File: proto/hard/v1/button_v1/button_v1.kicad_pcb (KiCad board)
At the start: 2 copper layers, 108.9 x 76.9 mm, 140 parts, among them J1 Conn_01x06_Female, J10 Conn_01x01_Female, J11 Conn_01x01_Female, J12 Conn_01x01_Female, J13 Conn_01x01_Female, J14 K3-2336D-combi, J15 Conn_01x03_Male, J16 Conn_01x01_Male, J2 Conn_01x06_Female, J3 Conn_01x06_Female, J4 Conn_01x06_Female, J5 USB_B_Micro, J6 Conn_01x08_Female, J7 Conn_01x04_Female, J8 AudioJack3, J9 Conn_01x01_Female, Q1 TP0610T, Q2 IRLML2060, Q3 TP0610T, Q4 IRLML2060, Q5 IRLML2060, Q6 UMG8N, Q7 UMG8N, Q8 TP0610T, U1 LCD_2.8_SPI, U10 NL27WZ14, U11 TC305, U12 OLED_0.96_I2C, U13 74HC595, U2 STM32F103C8Tx, U3 RT8009-33, U4 RClamp0554S, U5 RT9293, U7 AP1117-33, U8 485, U9 LM358, Y1 8MHz

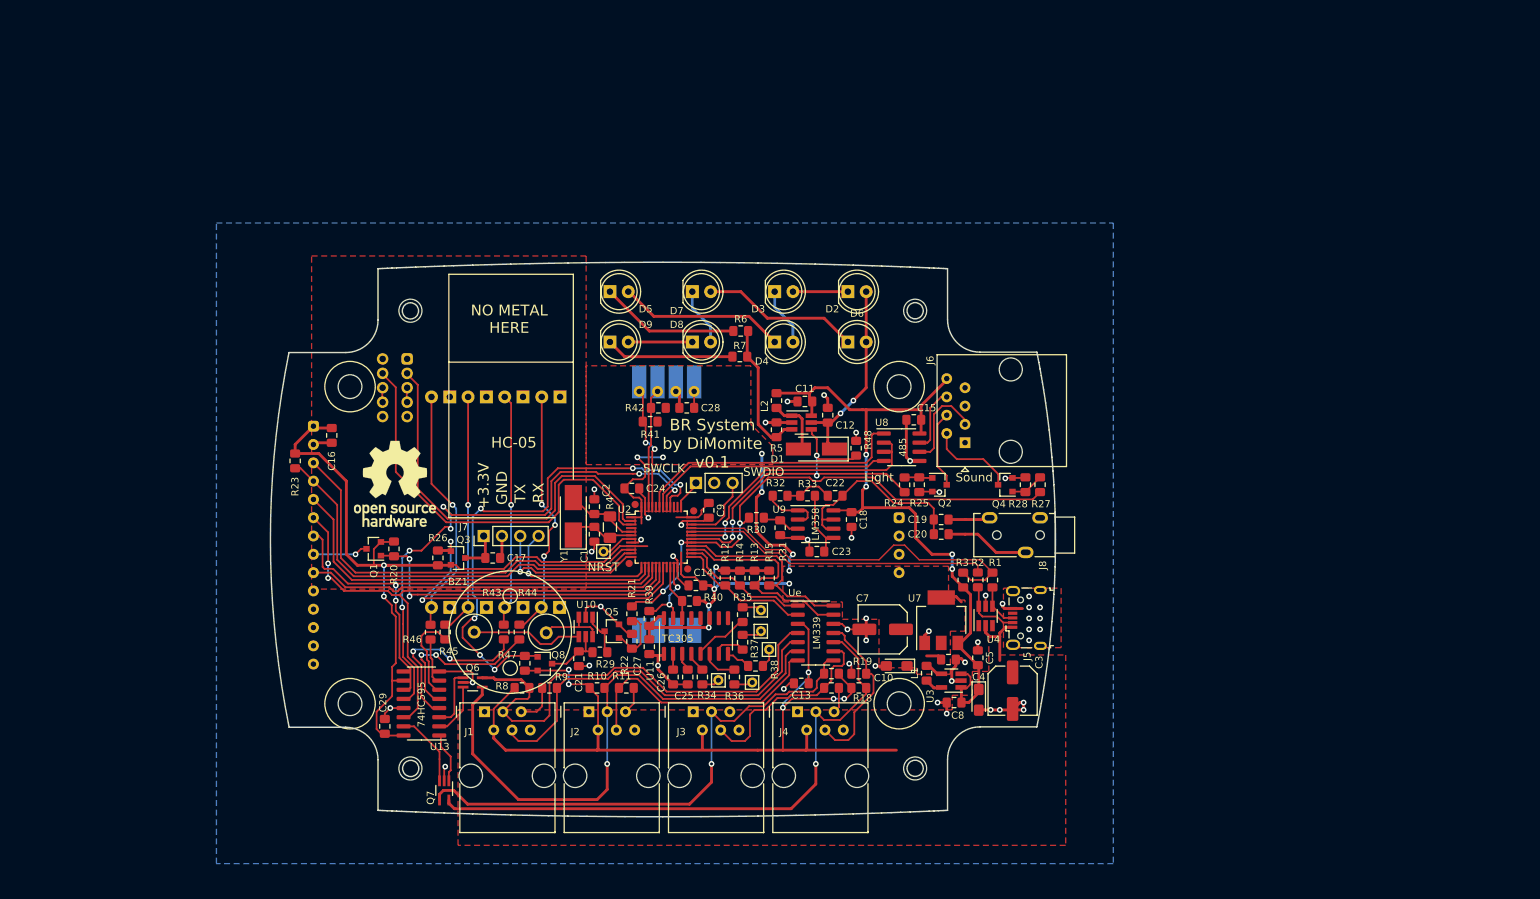
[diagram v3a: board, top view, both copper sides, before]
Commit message: Started schematic and PCB rework. Generated button_v1.pdf was left out of sync intentionally.
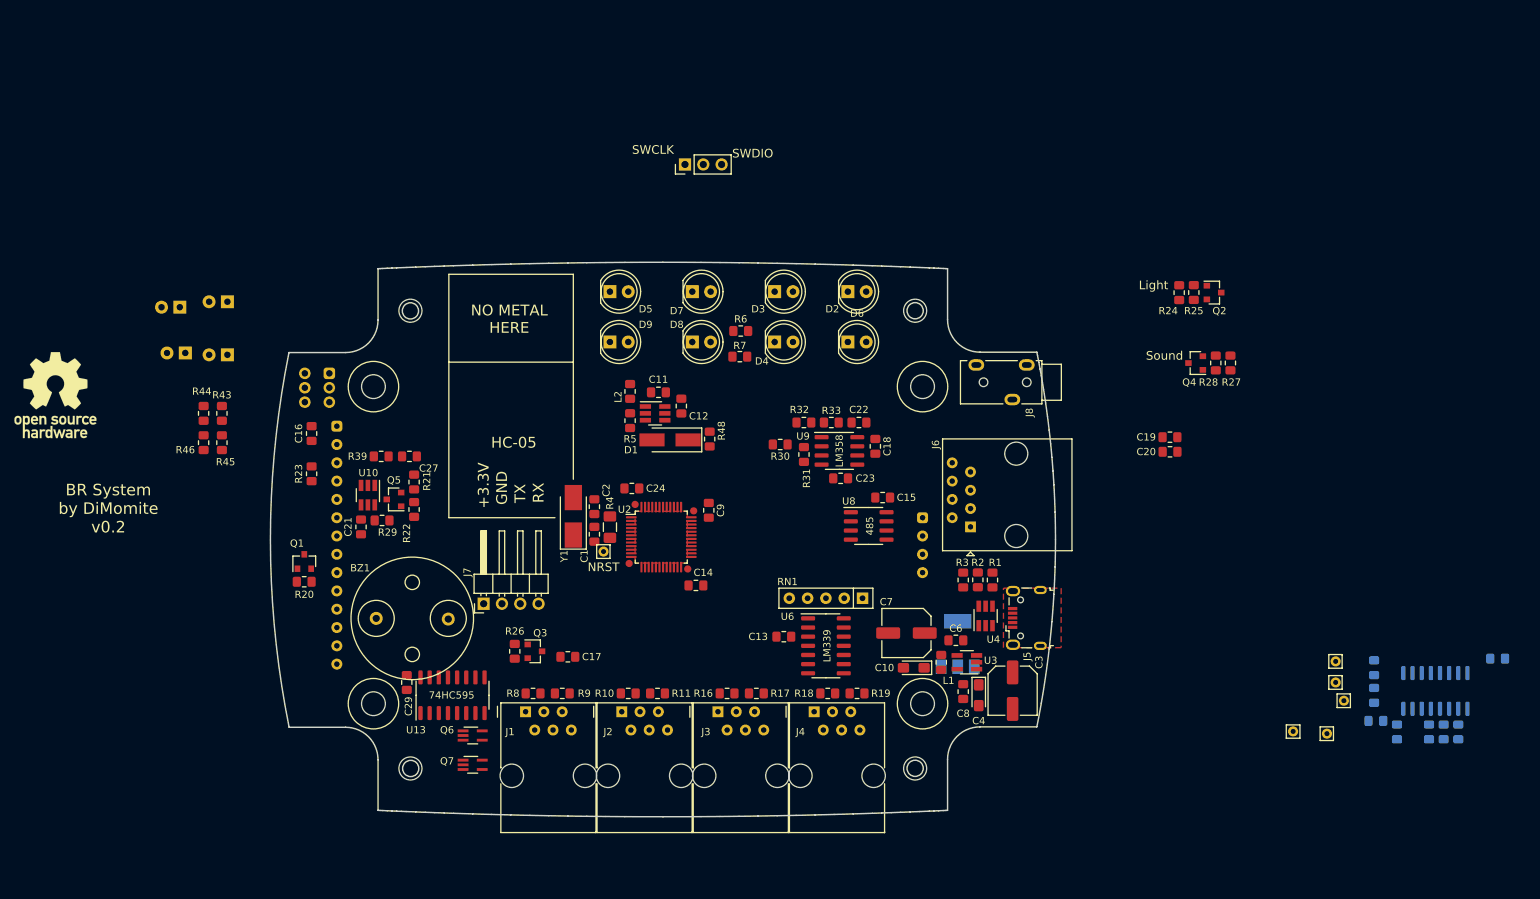
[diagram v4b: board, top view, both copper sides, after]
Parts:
- removed C28: 0.1uF, Capacitor_SMD:C_0805_2012Metric_Pad1.15x1.40mm_HandSolder
- removed C5: 1uF, Capacitor_SMD:C_0805_2012Metric_Pad1.15x1.40mm_HandSolder
- removed D14, D15, D16, D17: LED, LED_THT:LED_D3.0mm_Clear
- removed Q8: TP0610T, Package_TO_SOT_SMD:SOT-23
- removed R12, R13, R14, R15, R41, R42: 4k7, Resistor_SMD:R_0805_2012Metric_Pad1.15x1.40mm_HandSolder
- removed R47: 47k, Resistor_SMD:R_0805_2012Metric_Pad1.15x1.40mm_HandSolder
- removed U12: OLED_0.96_I2C, MyModules:OLED_0.96_I2C
- added RN1: 4k7, Resistor_THT:R_Array_SIP5, F.Cu at (150.6, 100.3)
- C25, C26, R34, R35, R36, R37, R38, R40, U11, U7: moved to B.Cu
- J14: value K3-2336D-combi -> K3-2235D; footprint brbuttonsystem:K3-2346D -> brbuttonsystem:K3-2235D
- J7: footprint Connector_PinHeader_2.54mm:PinHeader_1x04_P2.54mm_Vertical -> Connector_PinHeader_2.54mm:PinHeader_1x04_P2.54mm_Horizontal
- moved R40 112.4 mm to (238.8, 108.7)
- moved C26 109.2 mm to (233.3, 118.9)
- moved C25 105.2 mm to (231.3, 118.9)
- moved U11 102.9 mm to (230.1, 113.2)
- moved R34 101.1 mm to (229.2, 118.9)
- moved R36 92.3 mm to (224.8, 118.9)
- moved R35 87.9 mm to (221.6, 110.0)
- moved R37 87.9 mm to (221.6, 113.8)
- moved R38 86.4 mm to (221.9, 117.3), turned to 180 degrees
- moved J10 80.1 mm to (216.3, 109.1)
- moved J11 80.1 mm to (215.1, 119.1)
- moved J12 80.1 mm to (216.3, 112.0)
- moved J13 80.1 mm to (217.4, 114.6)
- moved J9 80.1 mm to (210.4, 118.8)
- moved D10 58.7 mm to (56.6, 66.3)
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- renumbered Ue to U6
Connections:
- C21 pad 1: /Entertainment/BuzzerPower -> Net-(C21-Pad1)
- J14 pad 4: Net-(J14-Pad4) -> GND
- J14 pad 5: GND -> Net-(J14-Pad5)
- J14 pad 6: Net-(J14-Pad10) -> Net-(J14-Pad6)
- Q6 pad 4: Net-(J2-Pad3) -> Net-(J2-Pad4)
- Q6 pad 5: Net-(J1-Pad3) -> Net-(J1-Pad4)
- Q7 pad 4: Net-(J3-Pad3) -> Net-(J4-Pad4)
- Q7 pad 5: Net-(J4-Pad3) -> Net-(J3-Pad4)
- R29 pad 2: /Entertainment/BuzzerPower -> +5V
- U10 pad 5: /Entertainment/BuzzerPower -> +5V
- U2 pad 3: /Touch4Front -> Net-(U2-Pad3)
- U2 pad 40: /BuzzerEnable -> Net-(U2-Pad40)
- U2 pad 45: /DISP_SCL -> Net-(U2-Pad45)
- U2 pad 46: /DISP_SDA -> Net-(U2-Pad46)
- U6 pad 10: Net-(J4-Pad3) -> Net-(J4-Pad4)
- U6 pad 11: Net-(J4-Pad4) -> Net-(J4-Pad3)
- U6 pad 4: Net-(J1-Pad3) -> Net-(J1-Pad4)
- U6 pad 5: Net-(J1-Pad4) -> Net-(J1-Pad3)
- U6 pad 6: Net-(J2-Pad3) -> Net-(J2-Pad4)
- U6 pad 7: Net-(J2-Pad4) -> Net-(J2-Pad3)
- U6 pad 8: Net-(J3-Pad3) -> Net-(J3-Pad4)
- U6 pad 9: Net-(J3-Pad4) -> Net-(J3-Pad3)
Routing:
- net +5V: track 236.4 -> 0.00 mm, vias 10 -> 0
- net +3V3: track 210.8 -> 0.00 mm, vias 13 -> 0
- net GND: track 138.3 -> 0.00 mm, vias 47 -> 0
- net Net-(J4-Pad3): track 81.6 -> 0.00 mm, vias 1 -> 0
- net Net-(J2-Pad3): track 78.8 -> 0.00 mm, vias 1 -> 0
- net /LCD_MOSI: track 77.8 -> 0.00 mm, vias 2 -> 0
- net /EXTRA_TICK: track 75.0 -> 0.00 mm, vias 6 -> 0
- net /Sound_PWM: track 73.4 -> 0.00 mm, vias 4 -> 0
- net Net-(J3-Pad3): track 73.1 -> 0.00 mm, vias 1 -> 0
- net /LCD_SCK: track 70.6 -> 0.00 mm, vias 2 -> 0
- net /BuzzerEnable: track 70.5 -> 0.00 mm, vias 6 -> 0
- net Net-(J1-Pad3): track 66.6 -> 0.00 mm
- net /LCD_RESET: track 59.1 -> 0.00 mm
- net /Touch4Front: track 58.4 -> 0.00 mm
- net /LCD_CS: track 57.7 -> 0.00 mm
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- removed copper zone on F.Cu, net +5V
- removed copper zone on B.Cu, net GND
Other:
- board text added: "!!! Offset by 4 mm from center !!!"
- board text added: "BR System by DiMomite v0.2"
- board text removed: "BR System by DiMomite v0.1"

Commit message: PCB rework in progress. Centered main LCD. Added second LCD. Button connectors we shifted to the right.
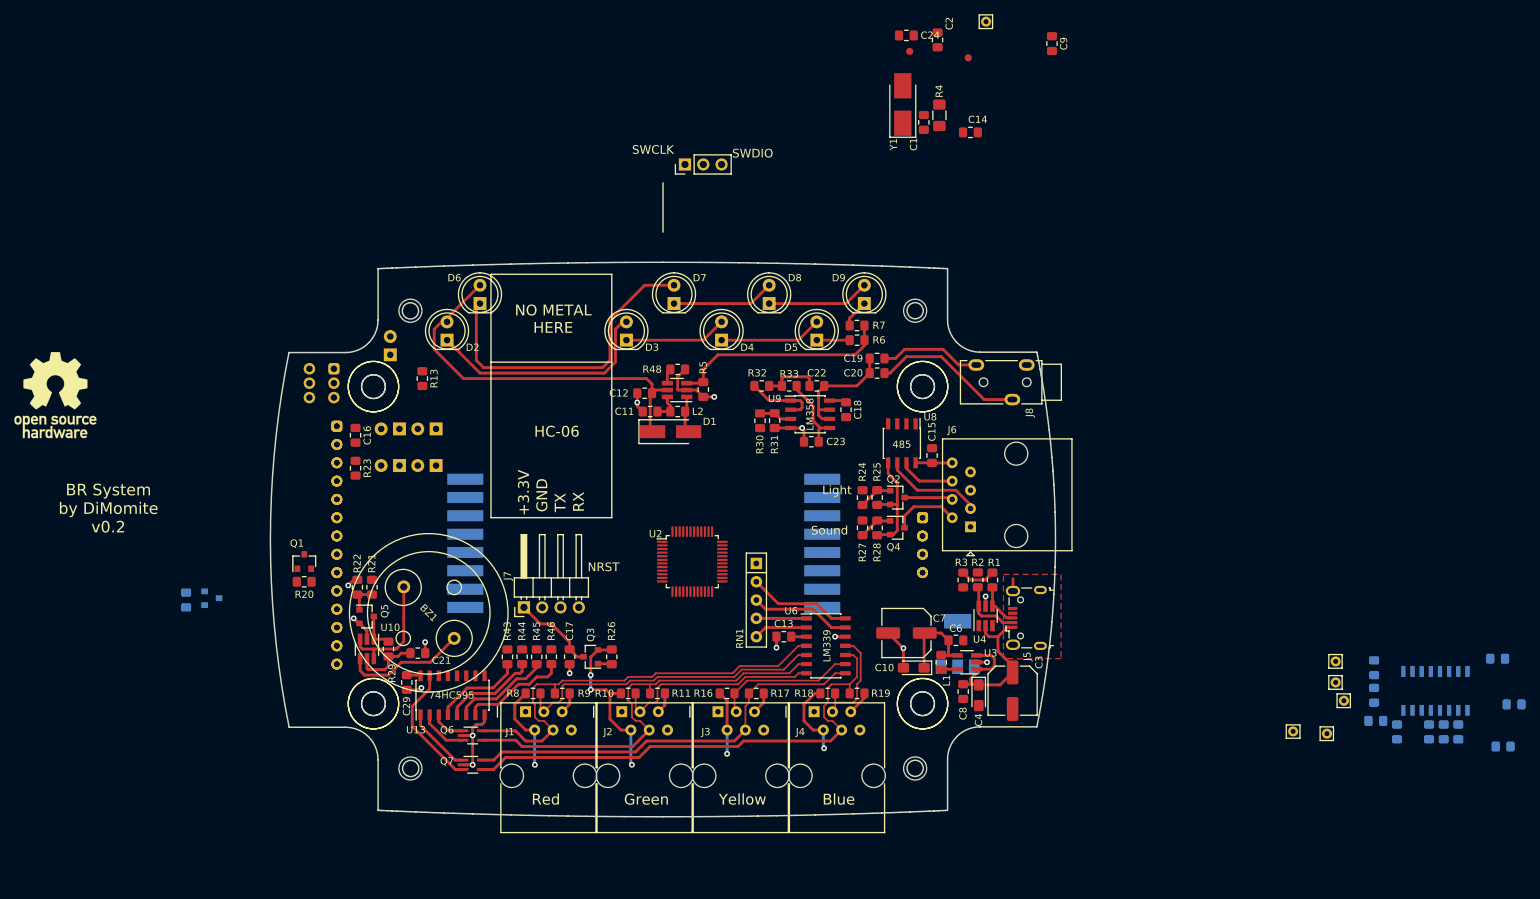
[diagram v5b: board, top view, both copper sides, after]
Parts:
- added D14: LED, LED_THT:LED_D3.0mm_Clear, B.Cu at (85.1, 66.5)
- added Q8: IRLML2803, Package_TO_SOT_SMD:SOT-23, B.Cu at (60.3, 100.3)
- added R12: 47k, Resistor_SMD:R_0805_2012Metric_Pad1.15x1.40mm_HandSolder, B.Cu at (56.8, 100.6)
- added R13: 1k, Resistor_SMD:R_0805_2012Metric_Pad1.15x1.40mm_HandSolder, F.Cu at (89.5, 69.8)
- added U1: LCD_2.8_SPI, MyModules:LCD_2.8_SPI, F.Cu at (77.7, 93.0)
- added U12: LCD_1_8_SPI, brbuttonsystem:LCD_1_8_SPI, B.Cu at (95.5, 92.7)
- BZ1: footprint MyModules:buzz17 -> brbuttonsystem:buzz17
- C27, R39: moved to B.Cu
- moved R39 160.9 mm to (241.0, 115.1)
- moved C27 157.0 mm to (239.5, 120.9)
- moved J16 90.7 mm to (167.8, 20.3)
- moved C9 80.4 mm to (176.9, 23.4)
- moved C2 80.4 mm to (161.0, 22.9)
- moved C14 73.5 mm to (165.6, 35.7)
- moved C24 73.5 mm to (156.7, 22.2)
- moved Y1 73.2 mm to (156.2, 31.8)
- moved C1 73.2 mm to (159.1, 34.3)
- moved R4 73.2 mm to (161.3, 33.3)
- moved R46 56.7 mm to (107.4, 108.4)
- moved D2 56.0 mm to (93.0, 64.5), turned to 90 degrees
- moved R27 55.9 mm to (150.6, 90.6), turned to 90 degrees
- moved R44 55.6 mm to (103.4, 108.4)
- moved R45 52.8 mm to (105.4, 108.5)
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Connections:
- net Net-(Q1-Pad3) renamed /MainLcdLed
- C21 pad 1: Net-(C21-Pad1) -> +5V
- J14 pad 4: GND -> Net-(J14-Pad4)
- J14 pad 6: Net-(J14-Pad6) -> GND
- J7 pad 3: /BT_RX -> /BTTX_MCURX
- J7 pad 4: /BT_TX -> /BTRX_MCUTX
- Q3 pad 2: +3V3 -> +5V
- R26 pad 1: +3V3 -> +5V
- U2 pad 12: /BT_RX -> /BTRX_MCUTX
- U2 pad 13: /BT_TX -> /BTTX_MCURX
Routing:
- net +5V: track 0.00 -> 107.2 mm, vias 0 -> 6
- net GND: track 0.00 -> 80.1 mm, vias 0 -> 15
- net Net-(J4-Pad4): track 0.00 -> 70.1 mm
- net Net-(J1-Pad4): track 0.00 -> 60.3 mm
- net Net-(J2-Pad4): track 0.00 -> 59.5 mm
- net Net-(J3-Pad4): track 0.00 -> 57.8 mm
- net /Entertainment/StartLedOut: track 0.00 -> 53.3 mm
- net Net-(D6-Pad1): track 0.00 -> 43.9 mm
- net Net-(J1-Pad3): track 0.00 -> 43.7 mm
- net Net-(D2-Pad1): track 0.00 -> 32.4 mm
- net Net-(R5-Pad2): track 0.00 -> 30.6 mm
- net Net-(J2-Pad3): track 0.00 -> 29.4 mm
- net Net-(C20-Pad1): track 0.00 -> 21.2 mm
- net Net-(J3-Pad3): track 0.00 -> 19.5 mm
- net /PLAY_LED0: track 0.00 -> 17.3 mm
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- removed copper zone on F.Cu, net +3V3
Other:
- board text added: "Blue"
- board text added: "Green"
- board text added: "HC-06"
- board text added: "Red"
- board text added: "Yellow"
- board text removed: "HC-05"

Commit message: Finished main board PCB
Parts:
- removed J11, J12, J13: Conn_01x01_Female, Connector_Pin:Pin_D0.7mm_L6.5mm_W1.8mm_FlatFork
- removed J15: Conn_01x03_Male, Connector_PinHeader_2.54mm:PinHeader_1x03_P2.54mm_Vertical
- removed J16: Conn_01x01_Male, Connector_Pin:Pin_D0.7mm_L6.5mm_W1.8mm_FlatFork
- removed R35, R36, R37, R38: 3k, Resistor_SMD:R_0805_2012Metric_Pad1.15x1.40mm_HandSolder
- removed the REF** at (38.6, 72.1)
- removed the U1 at (77.7, 93.0)
- added Q9: TP0610T, Package_TO_SOT_SMD:SOT-23, F.Cu at (163.6, 100.6)
- added R14: 47k, Resistor_SMD:R_0805_2012Metric_Pad1.15x1.40mm_HandSolder, F.Cu at (163.6, 103.4)
- added R15: 47k, Resistor_SMD:R_0805_2012Metric_Pad1.15x1.40mm_HandSolder, F.Cu at (92.8, 76.5)
- added REF**: GND, Connector_Wire:SolderWirePad_1x01_Drill1mm, F.Cu at (91.9, 127.0)
- added REF**: Light, TestPoint:TestPoint_Pad_1.5x1.5mm, F.Cu at (147.6, 85.3)
- added REF**: Sound, TestPoint:TestPoint_Pad_1.5x1.5mm, F.Cu at (148.0, 89.5)
- added REF**: 5V, TestPoint:TestPoint_Pad_1.5x1.5mm, F.Cu at (155.7, 119.3)
- added REF**: GND, Connector_Wire:SolderWirePad_1x01_Drill1mm, F.Cu at (166.1, 75.7)
- added REF**: 3.3V, TestPoint:TestPoint_Pad_1.5x1.5mm, F.Cu at (154.3, 100.1)
- added REF**: MountingHole_3.2mm_M3, MountingHole:MountingHole_3.2mm_M3, F.Cu at (71.9, 85.7)
- added REF**: MountingHole_3.2mm_M3, MountingHole:MountingHole_3.2mm_M3, F.Cu at (71.9, 98.7)
- added REF**: OSHW-Logo_7.5x8mm_SilkScreen, Symbol:OSHW-Logo_7.5x8mm_SilkScreen, F.Cu at (121.2, 105.7)
- added RN2: 3k, Resistor_SMD:R_Array_Convex_4x0603, B.Cu at (140.5, 110.8)
- C27, R39, R40, U11: moved to F.Cu
- J10: value Conn_01x01_Female -> Conn_01x04_Male; footprint Connector_Pin:Pin_D0.7mm_L6.5mm_W1.8mm_FlatFork -> Connector_PinHeader_2.54mm:PinHeader_1x04_P2.54mm_Vertical
- J9: value Conn_01x01_Female -> Conn_01x06_Male; footprint Connector_Pin:Pin_D0.7mm_L6.5mm_W1.8mm_FlatFork -> brbuttonsystem:A1501WR-S-5P; moved to B.Cu
- moved C27 115.9 mm to (125.2, 101.9), turned to 90 degrees
- moved R39 113.7 mm to (128.5, 98.7), turned to 0 degrees
- moved R40 106.8 mm to (132.5, 98.7)
- moved C26 105.1 mm to (128.5, 110.7)
- moved C25 101.0 mm to (130.6, 110.7)
- moved U11 98.5 mm to (132.1, 103.5)
- moved J10 93.5 mm to (131.1, 70.6)
- moved R34 88.9 mm to (140.5, 113.7), turned to 0 degrees
- moved C9 84.0 mm to (125.9, 90.0)
- moved C2 74.3 mm to (121.3, 85.6)
- moved Y1 67.5 mm to (118.2, 87.6)
- moved C1 67.1 mm to (121.3, 89.7)
- moved C24 66.5 mm to (127.1, 81.8), turned to 90 degrees
- moved C14 66.0 mm to (136.1, 94.8), turned to 270 degrees
- moved R4 65.7 mm to (123.5, 87.0)
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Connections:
- J10 pad 1: /CX1 -> /SWCLK
- Q8 pad 1: Net-(Q8-Pad1) -> /MainLcdLed
- R12 pad 2: Net-(Q8-Pad1) -> /MainLcdLed
- R3 pad 2: +5V -> Net-(Q9-Pad3)
- U12 pad 2: Net-(U12-Pad2) -> /LCD_RESET
- U12 pad 3: Net-(U12-Pad3) -> /BACK_LCD_CS
- U2 pad 10: /LCD_CS -> /EXTRA_TICK
- U2 pad 3: Net-(U2-Pad3) -> /LCD_CS
- U2 pad 38: Net-(U2-Pad38) -> /USB_PULLUP
- U2 pad 4: Net-(U2-Pad4) -> /BACK_LCD_CS
- U2 pad 41: /EXTRA_TICK -> Net-(U2-Pad41)
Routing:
- net +3V3: track 14.9 -> 288.1 mm, vias 0 -> 15
- net +5V: track 107.2 -> 352.5 mm, vias 6 -> 15
- net /Sound_PWM: track 0.00 -> 120.2 mm, vias 0 -> 4
- net /LCD_MOSI: track 0.00 -> 95.9 mm, vias 0 -> 4
- net /LCD_SCK: track 0.00 -> 87.0 mm, vias 0 -> 3
- net /LCD_DC: track 0.00 -> 69.9 mm, vias 0 -> 1
- net /LCD_RESET: track 0.00 -> 67.7 mm, vias 0 -> 1
- net /LCD_MISO: track 0.00 -> 63.5 mm, vias 0 -> 2
- net /LCD_CS: track 0.00 -> 59.4 mm
- net /EXTRA_TICK: track 0.00 -> 58.0 mm, vias 0 -> 2
- net /StartLed: track 2.08 -> 54.8 mm, vias 0 -> 5
- net /LCD_LED: track 0.00 -> 49.6 mm
- net Net-(D11-Pad2): track 0.00 -> 46.3 mm, vias 0 -> 2
- net /USB_PULLUP: track 0.00 -> 45.6 mm, vias 0 -> 2
- net /TouchEnable: track 0.00 -> 45.5 mm
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- added copper zone on F.Cu, net +5V
- added copper zone on B.Cu, net GND
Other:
- board text added: "CLK"
- board text added: "DIO"
- board text added: "RST"
- board text removed: "CX0"
- board text removed: "CX1"
- board text removed: "CX2"
- board text removed: "CX3"
- board text removed: "CX4"
- board text removed: "Light"
- board text removed: "NRST"
- board text removed: "SWCLK"
- board text removed: "SWDIO"
- board text removed: "Sound"

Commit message: Finised and reviewed v2 of main board. Schematic pdf, BOM and gerber archive are updated.
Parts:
- added REF**: GND, Connector_Wire:SolderWirePad_1x01_Drill1mm, F.Cu at (72.9, 71.4)
- moved R32 1.28 mm to (137.4, 71.9), turned to 270 degrees
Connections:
- net /EXTRA_TICK renamed /BACK_LED_CS
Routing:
- net +3V3: track 288.1 -> 264.6 mm, vias 15 -> 17
- net +5V: track 352.5 -> 343.1 mm, vias 15 -> 11
- net GND: track 124.9 -> 129.9 mm, vias 35 -> 37
- net /LCD_LED: track 49.6 -> 46.4 mm
- net Net-(R32-Pad2): track 10.0 -> 7.39 mm
- net Net-(D13-Pad2): track 44.7 -> 43.3 mm
- net /EXT_RW: track 31.7 -> 30.5 mm
- net /EXT_WRITE: track 27.9 -> 26.7 mm
- net /EXT_READ: track 37.2 -> 36.4 mm
- net /LCD_MOSI: track 95.9 -> 95.1 mm
- net /Entertainment/Sound_Analog: track 16.7 -> 17.5 mm, vias 0 -> 2
- net /LCD_RESET: track 67.7 -> 68.4 mm
- net /BTRX_MCUTX: track 26.3 -> 26.9 mm
- net Net-(C17-Pad1): track 11.9 -> 11.3 mm
- added copper zone on B.Cu, net +3V3
- added copper zone on F.Cu, net +3V3
- removed copper zone on F.Cu, net GND
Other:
- board text added: "Bluetooth HC-06"
- board text removed: "HC-06"
